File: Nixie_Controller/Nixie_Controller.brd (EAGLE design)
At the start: 150 x 100 mm, 59 parts, among them IC1 4028N, T1 MMBTA42, T10 MMBTA42, T11 MMBTA42, T12 MMBTA42, T13 MMBTA42, T14 MMBTA42, T2 MMBTA42, T3 MMBTA42, T4 MMBTA42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

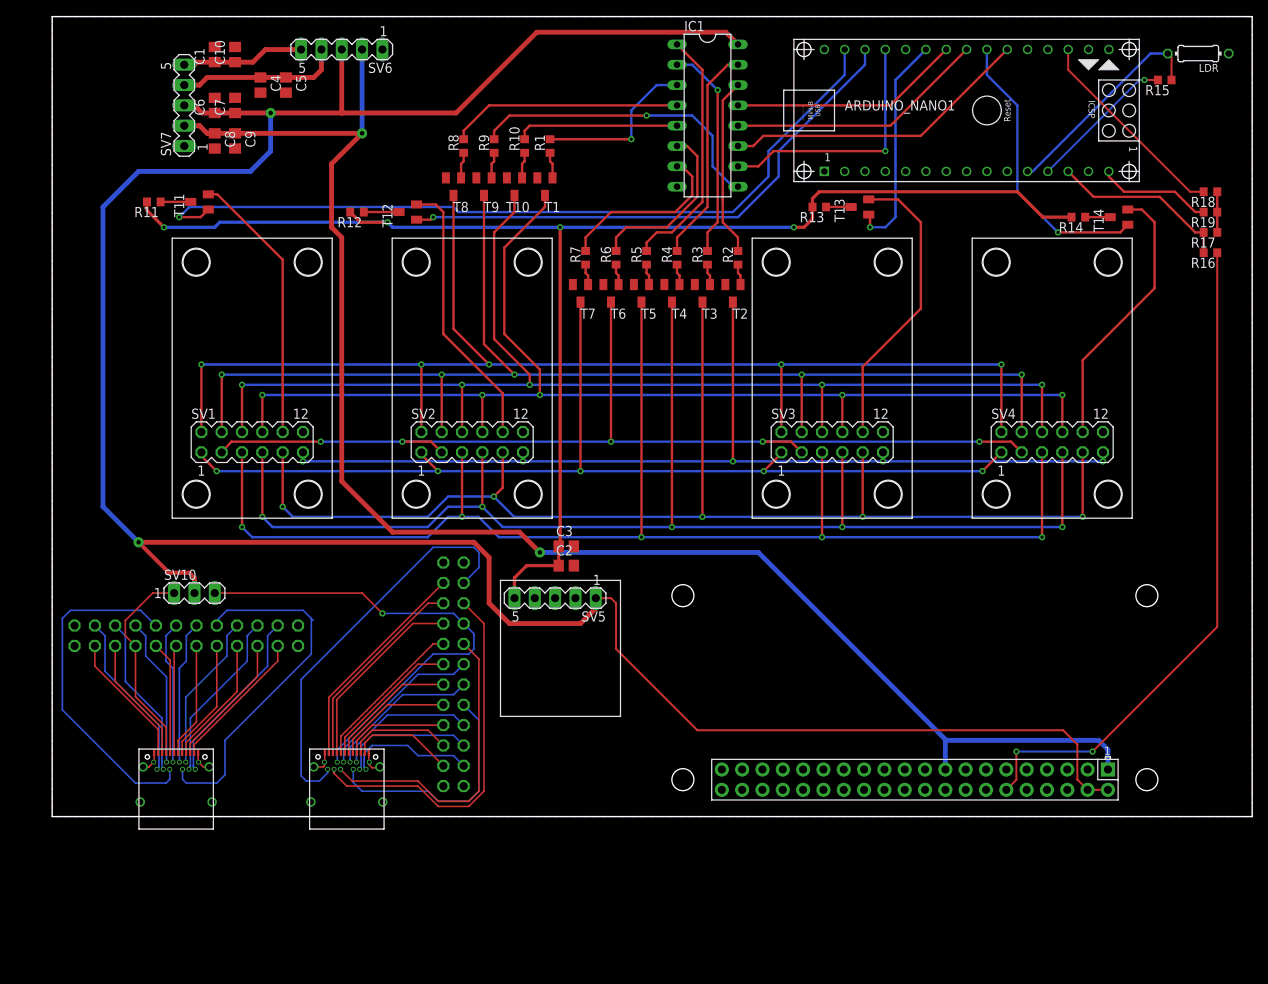
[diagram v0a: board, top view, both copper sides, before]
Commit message: fix: add zero ohms to supplies
Add a zero ohm resistor between the Arduino 3.3V and the 3.3V supply voltage.
Add a zero ohm resistor between the raspberry pi 5V and 3.3V and their respective supply voltages.
Remove the second connection to the arduino reset, because they are internally connected
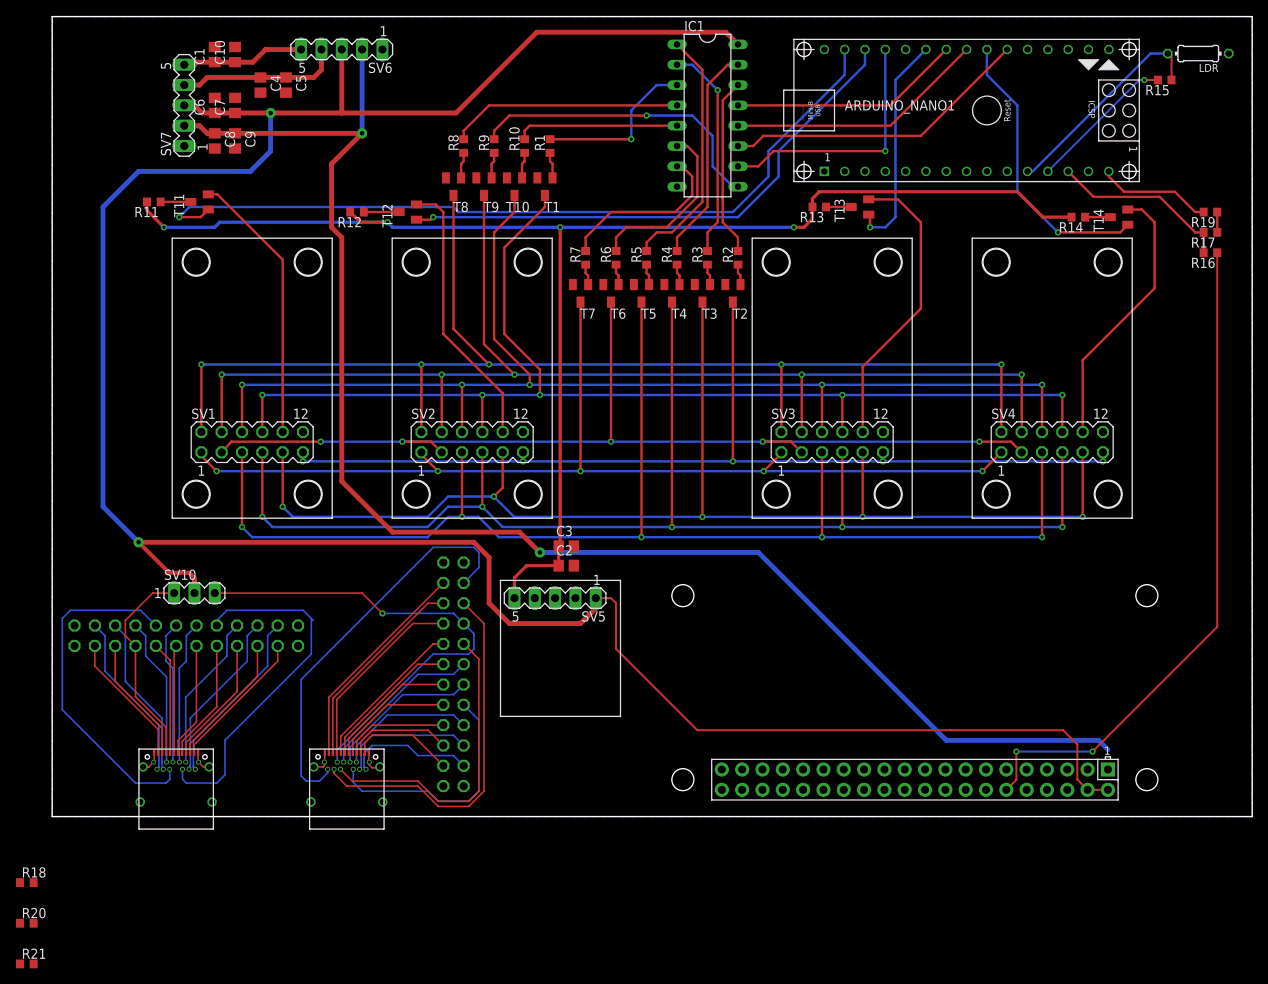
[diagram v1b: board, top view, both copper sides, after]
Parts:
- added R20, R21: 0, resistor:R0603
- R18: value 10k -> 0
- moved R18 171.3 mm to (-3.17, -8.26), turned to 0 degrees
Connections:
- removed net N$95: ARDUINO_NANO1.18, R18.2
- new net 3V3@2: R20.2, U$1.1, U$1.17
- new net N$39: ARDUINO_NANO1.1, R21.2
- net +3V3: now also R20.1, R21.1; no longer U$1.1, U$1.17
- net VDD: now also R18.2
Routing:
- net N$95: track 25.8 -> 0.00 mm
- net +3V3: track 194.6 -> 188.4 mm
- net +5V: track 5.08 -> 2.54 mm
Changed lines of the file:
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@@
 <element name="R16" library="resistor" package="R0603" value="0" x="144.78" y="70.485" rot="R180"/>
 <element name="R17" library="resistor" package="R0603" value="10k" x="144.78" y="73.025" rot="R180"/>
-<element name="R18" library="resistor" package="R0603" value="10k" x="144.78" y="78.105" rot="R180"/>
 <element name="R19" library="resistor" package="R0603" value="0" x="144.78" y="75.565" rot="R180"/>
+<element name="R18" library="resistor" package="R0603" value="0" x="-3.175" y="-8.255"/>
+<element name="R20" library="resistor" package="R0603" value="0" x="-3.175" y="-13.335"/>
+<element name="R21" library="resistor" package="R0603" value="0" x="-3.175" y="-18.415"/>
 </elements>
 <signals>
@@
 <wire x1="84.201" y1="98.044" x2="60.579" y2="98.044" width="0.6096" layer="1"/>
 <wire x1="60.579" y1="98.044" x2="50.485" y2="87.95" width="0.6096" layer="1"/>
+<contactref element="R18" pad="2"/>
+<wire x1="-2.325" y1="-8.255" x2="17.78" y2="27.94" width="0" layer="19" extent="1-1"/>
 </signal>
 <signal name="N$1">
@@
 <contactref element="C8" pad="1"/>
 <contactref element="C9" pad="1"/>
-<contactref element="U$1" pad="1"/>
-<contactref element="U$1" pad="17"/>
 <contactref element="SV6" pad="2"/>
 <wire x1="16.51" y1="86.36" x2="18.415" y2="86.36" width="0.6096" layer="1"/>
@@
 <wire x1="60.96" y1="33.02" x2="88.265" y2="33.02" width="0.6096" layer="16"/>
 <wire x1="111.645" y1="9.64" x2="88.265" y2="33.02" width="0.6096" layer="16"/>
-<wire x1="111.645" y1="9.64" x2="111.645" y2="5.885" width="0.6096" layer="16"/>
-<wire x1="131.965" y1="5.885" x2="131.965" y2="8.37" width="0.6096" layer="16"/>
 <wire x1="131.965" y1="8.37" x2="130.81" y2="9.525" width="0.6096" layer="16"/>
 <wire x1="130.81" y1="9.525" x2="111.76" y2="9.525" width="0.6096" layer="16"/>
@@
 <wire x1="36.195" y1="72.39" x2="36.195" y2="41.91" width="0.6096" layer="1"/>
 <wire x1="36.195" y1="41.91" x2="42.545" y2="35.56" width="0.6096" layer="1"/>
+<contactref element="R21" pad="1"/>
+<contactref element="R20" pad="1"/>
+<wire x1="-4.025" y1="-13.335" x2="42.545" y2="35.56" width="0" layer="19" extent="1-1"/>
+<wire x1="-4.025" y1="-18.415" x2="-4.025" y2="-13.335" width="0" layer="19" extent="1-1"/>
 </signal>
 <signal name="N$122">
@@
 <wire x1="145.63" y1="23.71" x2="145.63" y2="70.485" width="0.254" layer="1"/>
 </signal>
-<signal name="N$95">
-<contactref element="ARDUINO_NANO1" pad="18"/>
-<contactref element="R18" pad="2"/>
-<wire x1="143.93" y1="78.105" x2="142.24" y2="78.105" width="0.254" layer="1"/>
-<wire x1="127" y1="93.345" x2="127" y2="95.885" width="0.254" layer="1"/>
-<wire x1="142.24" y1="78.105" x2="127" y2="93.345" width="0.254" layer="1"/>
-</signal>
 <signal name="+5V">
 <contactref element="R17" pad="1"/>
+<contactref element="R19" pad="1"/>
+<wire x1="145.63" y1="75.565" x2="145.63" y2="73.025" width="0.3048" layer="1"/>
 <contactref element="R18" pad="1"/>
-<contactref element="R19" pad="1"/>
-<wire x1="145.63" y1="78.105" x2="145.63" y2="75.565" width="0.3048" layer="1"/>
-<wire x1="145.63" y1="75.565" x2="145.63" y2="73.025" width="0.3048" layer="1"/>
+<wire x1="-4.025" y1="-8.255" x2="145.63" y2="73.025" width="0" layer="19" extent="1-1"/>
 </signal>
 <signal name="N$96">
@@
 <wire x1="132.08" y1="80.01" x2="132.08" y2="80.645" width="0.3048" layer="1"/>
 </signal>
+<signal name="N$39">
+<contactref element="ARDUINO_NANO1" pad="1"/>
+<contactref element="R21" pad="2"/>
+<wire x1="-2.325" y1="-18.415" x2="96.52" y2="80.645" width="0" layer="19" extent="1-1"/>
+</signal>
+<signal name="3V3@2">
+<contactref element="U$1" pad="1"/>
+<contactref element="U$1" pad="17"/>
+<contactref element="R20" pad="2"/>
+<wire x1="111.645" y1="5.885" x2="131.965" y2="5.885" width="0" layer="19" extent="1-1"/>
+<wire x1="-2.325" y1="-13.335" x2="111.645" y2="5.885" width="0" layer="19" extent="1-1"/>
+</signal>
 </signals>

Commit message: fix: add resistors from schematic fix
Add the three 0 ohm resistors to the board, which were added in the schematic fix
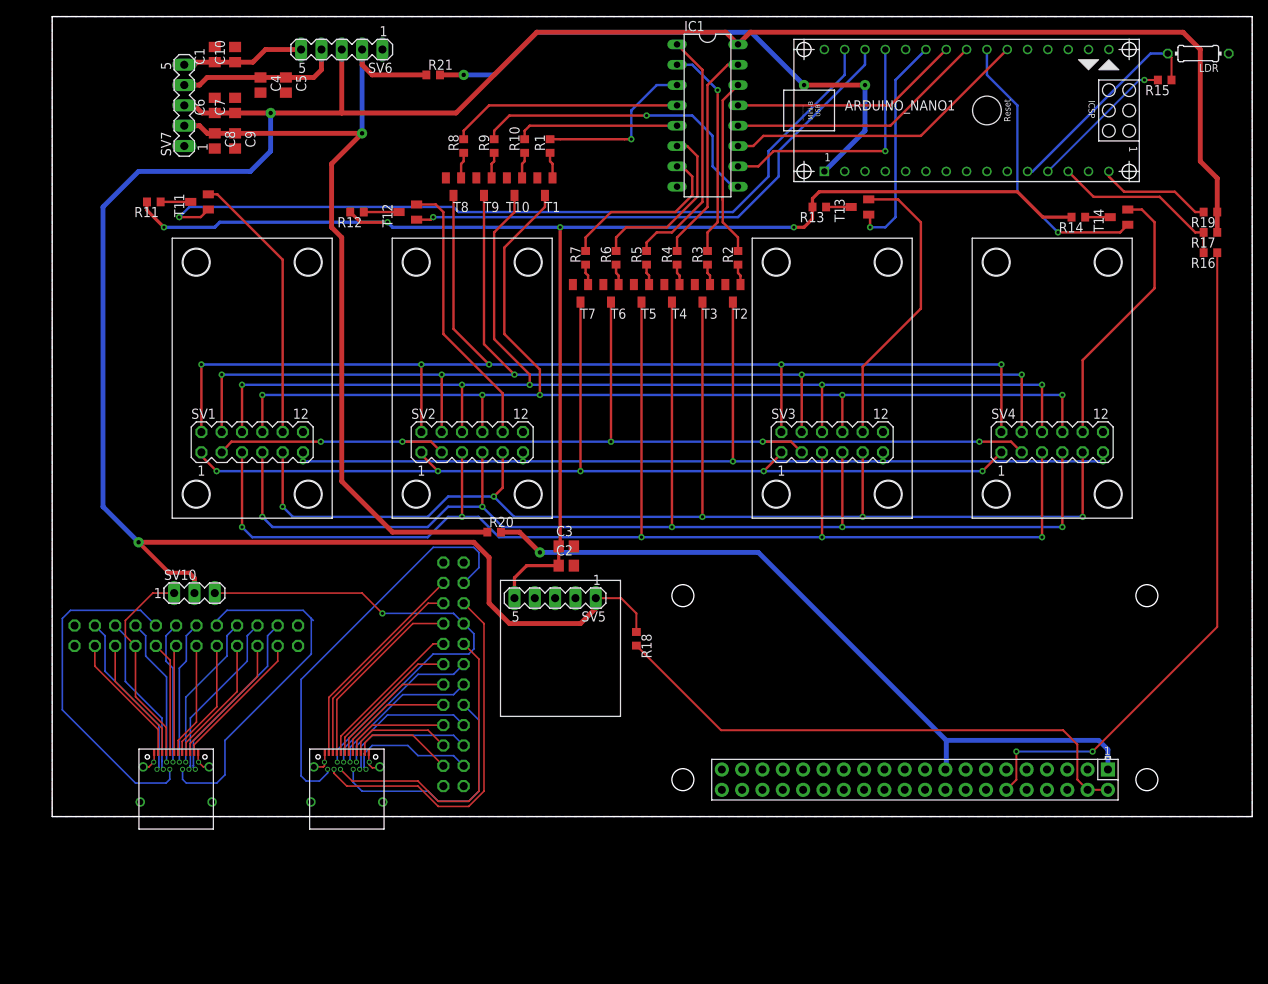
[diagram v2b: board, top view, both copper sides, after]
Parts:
- moved R21 122.2 mm to (47.6, 92.7)
- moved R18 82.1 mm to (73.0, 22.2), turned to 270 degrees
- moved R20 76.2 mm to (55.2, 35.6)
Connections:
- net +5V: now also R18.2, U$1.2, U$1.4; no longer R17.1, R18.1, R19.1
- net VDD: now also R17.1, R18.1, R19.1; no longer R18.2, U$1.2, U$1.4
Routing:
- net 3V3@2: track 0.00 -> 93.3 mm, vias 0 -> 1
- net +3V3: track 188.4 -> 110.0 mm, vias 2 -> 1
- net N$39: track 0.00 -> 71.0 mm, vias 0 -> 3
- net +5V: track 2.54 -> 69.0 mm
- net VDD: track 312.1 -> 323.5 mm
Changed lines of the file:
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@@
 <setting verticaltext="up"/>
 </settings>
-<grid distance="25" unitdist="mil" unit="mm" style="lines" multiple="1" display="no" altdistance="5" altunitdist="mil" altunit="mm"/>
+<grid distance="25" unitdist="mil" unit="mil" style="lines" multiple="1" display="no" altdistance="5" altunitdist="mil" altunit="mil"/>
 <layers>
 <layer number="1" name="Top" color="4" fill="1" visible="yes" active="yes"/>
@@
 <element name="R17" library="resistor" package="R0603" value="10k" x="144.78" y="73.025" rot="R180"/>
 <element name="R19" library="resistor" package="R0603" value="0" x="144.78" y="75.565" rot="R180"/>
-<element name="R18" library="resistor" package="R0603" value="0" x="-3.175" y="-8.255"/>
-<element name="R20" library="resistor" package="R0603" value="0" x="-3.175" y="-13.335"/>
-<element name="R21" library="resistor" package="R0603" value="0" x="-3.175" y="-18.415"/>
+<element name="R18" library="resistor" package="R0603" value="0" x="73.025" y="22.225" rot="R270"/>
+<element name="R20" library="resistor" package="R0603" value="0" x="55.245" y="35.56"/>
+<element name="R21" library="resistor" package="R0603" value="0" x="47.625" y="92.71"/>
 </elements>
 <signals>
@@
 <contactref element="C6" pad="1"/>
 <contactref element="C7" pad="1"/>
-<contactref element="U$1" pad="2"/>
-<contactref element="U$1" pad="4"/>
 <contactref element="SV6" pad="3"/>
 <contactref element="SV10" pad="2"/>
@@
 <wire x1="18.73" y1="87.95" x2="20.32" y2="87.95" width="0.6096" layer="1"/>
 <wire x1="20.32" y1="87.95" x2="22.86" y2="87.95" width="0.6096" layer="1"/>
-<wire x1="131.965" y1="3.345" x2="129.425" y2="3.345" width="0.254" layer="1"/>
-<wire x1="128.143" y1="9.017" x2="126.365" y2="10.795" width="0.254" layer="1"/>
-<wire x1="126.365" y1="10.795" x2="80.645" y2="10.795" width="0.254" layer="1"/>
-<wire x1="70.485" y1="20.955" x2="80.645" y2="10.795" width="0.254" layer="1"/>
-<wire x1="129.425" y1="3.345" x2="128.143" y2="4.627" width="0.254" layer="1"/>
-<wire x1="128.143" y1="4.627" x2="128.143" y2="9.017" width="0.254" layer="1"/>
 <wire x1="52.705" y1="34.29" x2="10.795" y2="34.29" width="0.6096" layer="1"/>
 <wire x1="52.705" y1="34.29" x2="54.61" y2="32.385" width="0.6096" layer="1"/>
@@
 <wire x1="67.945" y1="26.035" x2="67.945" y2="27.305" width="0.6096" layer="1"/>
 <wire x1="66.04" y1="24.13" x2="67.945" y2="26.035" width="0.6096" layer="1"/>
-<wire x1="67.945" y1="27.305" x2="69.85" y2="27.305" width="0.254" layer="1"/>
-<wire x1="69.85" y1="27.305" x2="70.485" y2="26.67" width="0.254" layer="1"/>
-<wire x1="70.485" y1="26.67" x2="70.485" y2="20.955" width="0.254" layer="1"/>
 <wire x1="10.795" y1="34.29" x2="14.605" y2="30.48" width="0.508" layer="1"/>
 <wire x1="17.145" y1="30.48" x2="17.78" y2="29.845" width="0.508" layer="1"/>
 <wire x1="14.605" y1="30.48" x2="17.145" y2="30.48" width="0.508" layer="1"/>
-<wire x1="85.725" y1="96.52" x2="84.201" y2="98.044" width="0.6096" layer="1"/>
+<wire x1="84.201" y1="98.044" x2="85.725" y2="96.52" width="0.6096" layer="1"/>
 <wire x1="84.201" y1="98.044" x2="60.579" y2="98.044" width="0.6096" layer="1"/>
 <wire x1="60.579" y1="98.044" x2="50.485" y2="87.95" width="0.6096" layer="1"/>
-<contactref element="R18" pad="2"/>
-<wire x1="-2.325" y1="-8.255" x2="17.78" y2="27.94" width="0" layer="19" extent="1-1"/>
+<contactref element="R17" pad="1"/>
+<contactref element="R19" pad="1"/>
+<contactref element="R18" pad="1"/>
+<wire x1="71.12" y1="27.305" x2="73.025" y2="25.4" width="0.254" layer="1"/>
+<wire x1="73.025" y1="25.4" x2="73.025" y2="23.075" width="0.254" layer="1"/>
+<wire x1="67.945" y1="27.305" x2="71.12" y2="27.305" width="0.254" layer="1"/>
+<wire x1="85.725" y1="96.52" x2="87.249" y2="98.044" width="0.6096" layer="1"/>
+<wire x1="143.51" y1="95.885" x2="143.51" y2="81.915" width="0.6096" layer="1"/>
+<wire x1="143.51" y1="81.915" x2="145.63" y2="79.795" width="0.6096" layer="1"/>
+<wire x1="145.63" y1="79.795" x2="145.63" y2="75.565" width="0.6096" layer="1"/>
+<wire x1="87.249" y1="98.044" x2="141.351" y2="98.044" width="0.6096" layer="1"/>
+<wire x1="141.351" y1="98.044" x2="143.51" y2="95.885" width="0.6096" layer="1"/>
+<wire x1="145.63" y1="75.565" x2="145.63" y2="73.025" width="0.6096" layer="1"/>
 </signal>
 <signal name="N$1">
@@
 <via x="38.735" y="85.405" extent="1-16" drill="0.55" diameter="1.3"/>
 <wire x1="38.735" y1="95.885" x2="38.735" y2="85.405" width="0.6096" layer="16"/>
-<via x="60.96" y="33.02" extent="1-16" drill="0.55" diameter="1.3"/>
-<wire x1="60.96" y1="33.02" x2="88.265" y2="33.02" width="0.6096" layer="16"/>
-<wire x1="111.645" y1="9.64" x2="88.265" y2="33.02" width="0.6096" layer="16"/>
-<wire x1="131.965" y1="8.37" x2="130.81" y2="9.525" width="0.6096" layer="16"/>
-<wire x1="130.81" y1="9.525" x2="111.76" y2="9.525" width="0.6096" layer="16"/>
-<wire x1="111.76" y1="9.525" x2="111.645" y2="9.64" width="0.6096" layer="16"/>
-<wire x1="58.42" y1="35.56" x2="60.96" y2="33.02" width="0.6096" layer="1"/>
-<wire x1="42.545" y1="35.56" x2="58.42" y2="35.56" width="0.6096" layer="1"/>
 <wire x1="38.735" y1="85.405" x2="34.925" y2="81.595" width="0.6096" layer="1"/>
 <wire x1="34.925" y1="81.595" x2="34.925" y2="73.66" width="0.6096" layer="1"/>
 <wire x1="34.925" y1="73.66" x2="36.195" y2="72.39" width="0.6096" layer="1"/>
 <wire x1="36.195" y1="72.39" x2="36.195" y2="41.91" width="0.6096" layer="1"/>
-<wire x1="36.195" y1="41.91" x2="42.545" y2="35.56" width="0.6096" layer="1"/>
+<wire x1="42.545" y1="35.56" x2="36.195" y2="41.91" width="0.6096" layer="1"/>
 <contactref element="R21" pad="1"/>
 <contactref element="R20" pad="1"/>
-<wire x1="-4.025" y1="-13.335" x2="42.545" y2="35.56" width="0" layer="19" extent="1-1"/>
-<wire x1="-4.025" y1="-18.415" x2="-4.025" y2="-13.335" width="0" layer="19" extent="1-1"/>
+<wire x1="54.395" y1="35.56" x2="42.545" y2="35.56" width="0.6096" layer="1"/>
+<wire x1="38.735" y1="95.885" x2="38.735" y2="93.98" width="0.6096" layer="1"/>
+<wire x1="38.735" y1="93.98" x2="40.005" y2="92.71" width="0.6096" layer="1"/>
+<wire x1="40.005" y1="92.71" x2="46.775" y2="92.71" width="0.6096" layer="1"/>
 </signal>
 <signal name="N$122">
@@
 <wire x1="145.63" y1="23.71" x2="145.63" y2="70.485" width="0.254" layer="1"/>
 </signal>
-<signal name="+5V">
-<contactref element="R17" pad="1"/>
-<contactref element="R19" pad="1"/>
-<wire x1="145.63" y1="75.565" x2="145.63" y2="73.025" width="0.3048" layer="1"/>
-<contactref element="R18" pad="1"/>
-<wire x1="-4.025" y1="-8.255" x2="145.63" y2="73.025" width="0" layer="19" extent="1-1"/>
-</signal>
 <signal name="N$96">
 <contactref element="R19" pad="2"/>
@@
 <contactref element="ARDUINO_NANO1" pad="1"/>
 <contactref element="R21" pad="2"/>
-<wire x1="-2.325" y1="-18.415" x2="96.52" y2="80.645" width="0" layer="19" extent="1-1"/>
+<wire x1="48.475" y1="92.71" x2="51.435" y2="92.71" width="0.6096" layer="1"/>
+<via x="51.435" y="92.71" extent="1-16" drill="0.55" diameter="1.3"/>
+<wire x1="51.435" y1="92.71" x2="55.245" y2="92.71" width="0.6096" layer="16"/>
+<via x="93.98" y="91.44" extent="1-16" drill="0.55" diameter="1.3"/>
+<wire x1="93.98" y1="91.44" x2="101.6" y2="91.44" width="0.6096" layer="1"/>
+<via x="101.6" y="91.44" extent="1-16" drill="0.55" diameter="1.3"/>
+<wire x1="101.6" y1="91.44" x2="101.6" y2="85.725" width="0.6096" layer="16"/>
+<wire x1="101.6" y1="85.725" x2="96.52" y2="80.645" width="0.6096" layer="16"/>
+<wire x1="55.245" y1="92.71" x2="60.579" y2="98.044" width="0.6096" layer="16"/>
+<wire x1="60.579" y1="98.044" x2="87.376" y2="98.044" width="0.6096" layer="16"/>
+<wire x1="87.376" y1="98.044" x2="93.98" y2="91.44" width="0.6096" layer="16"/>
 </signal>
 <signal name="3V3@2">
@@
 <contactref element="U$1" pad="17"/>
 <contactref element="R20" pad="2"/>
-<wire x1="111.645" y1="5.885" x2="131.965" y2="5.885" width="0" layer="19" extent="1-1"/>
-<wire x1="-2.325" y1="-13.335" x2="111.645" y2="5.885" width="0" layer="19" extent="1-1"/>
+<wire x1="56.095" y1="35.56" x2="58.42" y2="35.56" width="0.6096" layer="1"/>
+<wire x1="58.42" y1="35.56" x2="60.96" y2="33.02" width="0.6096" layer="1"/>
+<via x="60.96" y="33.02" extent="1-16" drill="0.55" diameter="1.3"/>
+<wire x1="60.96" y1="33.02" x2="88.265" y2="33.02" width="0.6096" layer="16"/>
+<wire x1="111.76" y1="9.525" x2="88.265" y2="33.02" width="0.6096" layer="16"/>
+<wire x1="131.965" y1="8.37" x2="131.965" y2="5.885" width="0.6096" layer="16"/>
+<wire x1="111.76" y1="9.525" x2="130.81" y2="9.525" width="0.6096" layer="16"/>
+<wire x1="130.81" y1="9.525" x2="131.965" y2="8.37" width="0.6096" layer="16"/>
+<wire x1="111.645" y1="5.885" x2="111.76" y2="6" width="0.6096" layer="16"/>
+<wire x1="111.76" y1="6" x2="111.76" y2="9.525" width="0.6096" layer="16"/>
+</signal>
+<signal name="+5V">
+<contactref element="U$1" pad="2"/>
+<contactref element="U$1" pad="4"/>
+<contactref element="R18" pad="2"/>
+<wire x1="129.425" y1="3.345" x2="131.965" y2="3.345" width="0.254" layer="1"/>
+<wire x1="73.025" y1="21.375" x2="83.605" y2="10.795" width="0.254" layer="1"/>
+<wire x1="83.605" y1="10.795" x2="126.365" y2="10.795" width="0.254" layer="1"/>
+<wire x1="126.365" y1="10.795" x2="128.143" y2="9.017" width="0.254" layer="1"/>
+<wire x1="128.143" y1="4.627" x2="129.425" y2="3.345" width="0.254" layer="1"/>
+<wire x1="128.143" y1="9.017" x2="128.143" y2="4.627" width="0.254" layer="1"/>
 </signal>
 </signals>
